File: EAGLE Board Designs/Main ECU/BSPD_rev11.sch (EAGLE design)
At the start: 55 parts, among them Q1 P-CHANNEL_MOSFET_DMP3099L-7, U11 SN74AHC1G09, U17 OPA990IDBVR, U19 OPA990IDBVR, U28 OPA990IDBVR, U29 OPA990IDBVR, U6 OPA990IDBVR, X1 CONNECTOR-4NANO-FIT-VERTICAL-4, X2 CONNECTOR-4NANO-FIT-VERTICAL-4

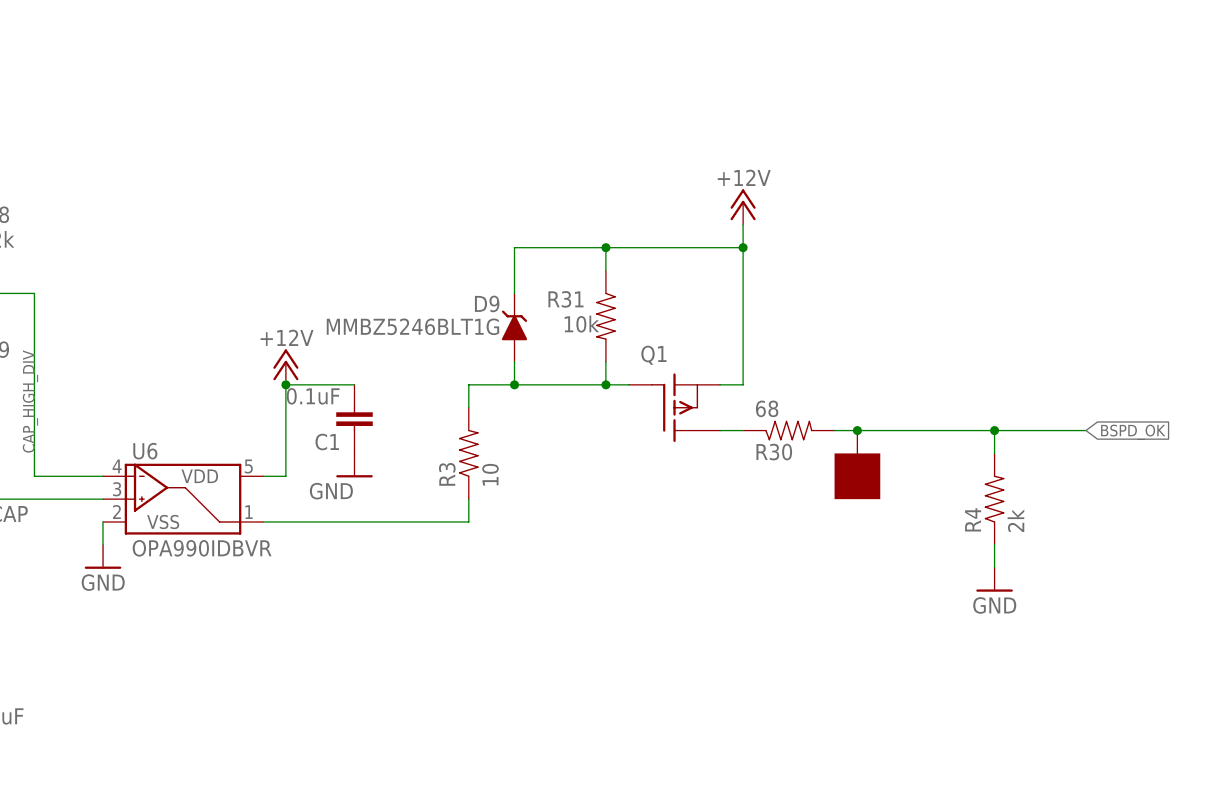
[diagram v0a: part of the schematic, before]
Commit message: Made layout more compact
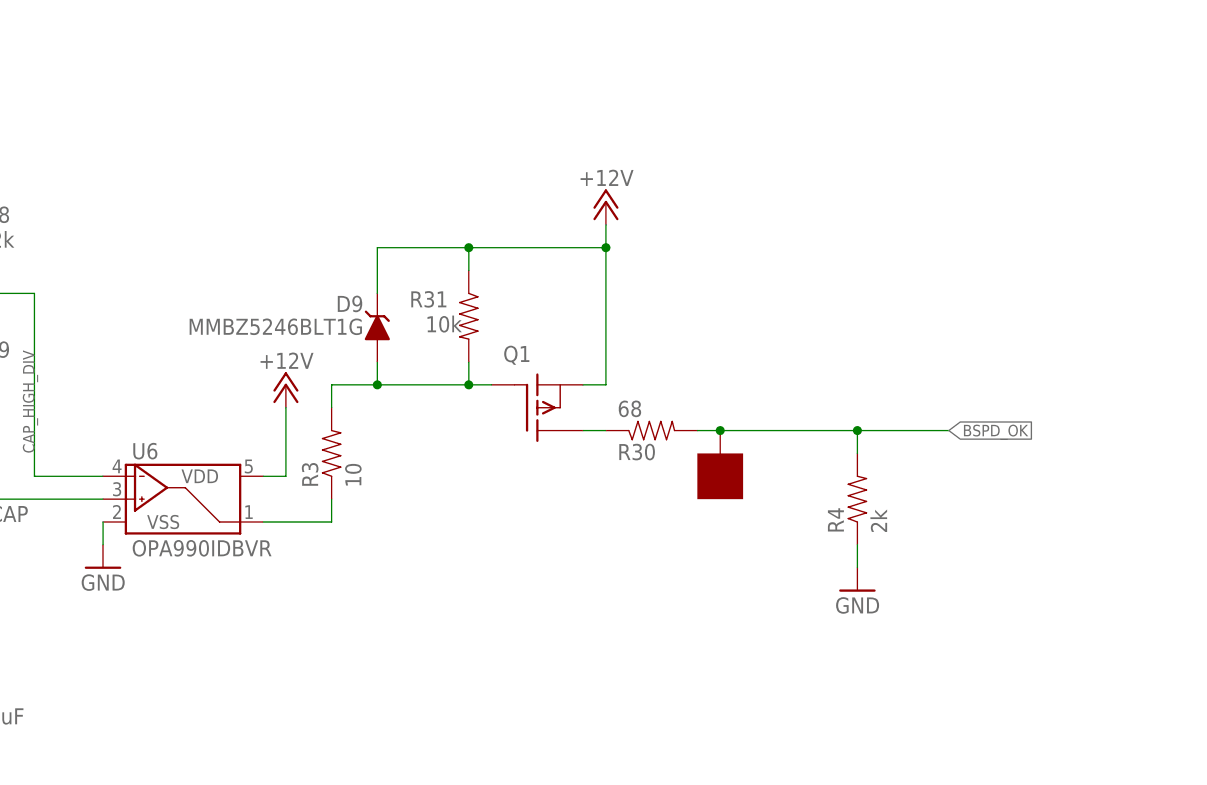
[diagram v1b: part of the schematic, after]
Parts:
- removed C1: 0.1uF, HyTechDevices:CAP0603-CAP
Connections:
- net +12V: no longer C1.2
- net GND: no longer C1.1
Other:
- moved on the sheet: D9, Q1, R3, R30, R31, R4

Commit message: Made more compact, adjusted labels
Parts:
- renumbered U$1 to BRAKE_LOW_DIV, U$2 to CURRENT_LOW_DIV
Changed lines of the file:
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@@
 <part name="R7" library="HyTechDevices" deviceset="RESISTOR" device="0603" value="31600"/>
 <part name="R8" library="HyTechDevices" deviceset="RESISTOR" device="0603" value="5110"/>
-<part name="U$1" library="HyTechDevices" deviceset="SOLDER_PAD" device=""/>
-<part name="U$2" library="HyTechDevices" deviceset="SOLDER_PAD" device=""/>
+<part name="BRAKE_LOW_DIV" library="HyTechDevices" deviceset="SOLDER_PAD" device=""/>
+<part name="CURRENT_LOW_DIV" library="HyTechDevices" deviceset="SOLDER_PAD" device=""/>
 </parts>
 <sheets>
@@
 <attribute name="VALUE" x="104.902" y="158.75" size="1.778" layer="96" rot="R90"/>
 </instance>
-<instance part="U$1" gate="G$1" x="154.94" y="157.48" smashed="yes" rot="R270"/>
-<instance part="U$2" gate="G$1" x="182.88" y="218.44" smashed="yes"/>
+<instance part="BRAKE_LOW_DIV" gate="G$1" x="154.94" y="157.48" smashed="yes" rot="R270"/>
+<instance part="CURRENT_LOW_DIV" gate="G$1" x="182.88" y="218.44" smashed="yes"/>
 </instances>
 <busses>
@@
 <wire x1="167.64" y1="226.06" x2="152.4" y2="226.06" width="0.1524" layer="91"/>
 <junction x="167.64" y="226.06"/>
-<pinref part="U$2" gate="G$1" pin="P$1"/>
+<pinref part="CURRENT_LOW_DIV" gate="G$1" pin="P$1"/>
 <junction x="180.34" y="220.98"/>
 </segment>
@@
 <pinref part="R6" gate="G$1" pin="2"/>
 <junction x="167.64" y="160.02"/>
-<pinref part="U$1" gate="G$1" pin="P$1"/>
+<pinref part="BRAKE_LOW_DIV" gate="G$1" pin="P$1"/>
 <junction x="157.48" y="160.02"/>
 </segment>

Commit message: Routed BSPD circuit, readjusted some components
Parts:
- renumbered U$3 to BSPD_OK
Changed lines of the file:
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@@
 <part name="P+2" library="HyTechSupplies" deviceset="+12V" device=""/>
 <part name="P+8" library="HyTechSupplies" deviceset="+12V" device=""/>
-<part name="U$3" library="HyTechDevices" deviceset="SOLDER_PAD" device=""/>
+<part name="BSPD_OK" library="HyTechDevices" deviceset="SOLDER_PAD" device=""/>
 <part name="R3" library="HyTechDevices" deviceset="RESISTOR" device="0603" value="10"/>
 <part name="REG2" library="HyTechDevices" deviceset="OKI-78SR-5" device="" value="5V"/>
@@
 <attribute name="VALUE" x="80.772" y="77.978" size="1.778" layer="96"/>
 </instance>
-<instance part="U$3" gate="G$1" x="365.76" y="167.64" smashed="yes" rot="R270"/>
+<instance part="BSPD_OK" gate="G$1" x="365.76" y="167.64" smashed="yes" rot="R270"/>
 <instance part="R3" gate="G$1" x="325.12" y="167.64" smashed="yes" rot="R90">
 <attribute name="NAME" x="323.6214" y="163.83" size="1.778" layer="95" rot="R90"/>
@@
 <wire x1="365.76" y1="170.18" x2="368.3" y2="170.18" width="0.1524" layer="91"/>
 <label x="393.7" y="170.18" size="1.27" layer="95" xref="yes"/>
-<pinref part="U$3" gate="G$1" pin="P$1"/>
+<pinref part="BSPD_OK" gate="G$1" pin="P$1"/>
 <junction x="368.3" y="170.18"/>
 <pinref part="R4" gate="G$1" pin="2"/>

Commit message: Changed GND of LEDs, cleaned up routing
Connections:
- removed net GND1: BRAKE.C, BSPD.C, CURRENT.C
- net GND: now also BRAKE.C, BSPD.C, CURRENT.C
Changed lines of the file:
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@@
 <part name="R4" library="HyTechDevices" deviceset="RESISTOR" device="0603" value="2k"/>
 <part name="GND2" library="HyTechSymbols" deviceset="GND" device=""/>
-<part name="GND96" library="HyTechSymbols" deviceset="GND" device=""/>
 <part name="BRAKE" library="HyTechDevices" deviceset="LED" device="-0805" value="Red"/>
 <part name="R35" library="HyTechDevices" deviceset="RESISTOR" device="0603" value="215"/>
@@
 <part name="BRAKE_LOW_DIV" library="HyTechDevices" deviceset="SOLDER_PAD" device=""/>
 <part name="CURRENT_LOW_DIV" library="HyTechDevices" deviceset="SOLDER_PAD" device=""/>
+<part name="GND5" library="HyTechSupplies" deviceset="GND" device=""/>
 </parts>
 <sheets>
@@
 <attribute name="VALUE" x="386.08" y="149.86" size="1.778" layer="96" rot="MR0"/>
 </instance>
-<instance part="GND96" gate="1" x="215.9" y="43.18" smashed="yes">
-<attribute name="VALUE" x="213.36" y="40.64" size="1.778" layer="96"/>
-</instance>
 <instance part="BRAKE" gate="LED" x="203.2" y="50.8" smashed="yes" rot="MR270">
 <attribute name="NAME" x="207.772" y="47.244" size="1.778" layer="95" rot="MR0"/>
@@
 <instance part="BRAKE_LOW_DIV" gate="G$1" x="154.94" y="157.48" smashed="yes" rot="R270"/>
 <instance part="CURRENT_LOW_DIV" gate="G$1" x="182.88" y="218.44" smashed="yes"/>
+<instance part="GND5" gate="1" x="215.9" y="43.18" smashed="yes">
+<attribute name="VALUE" x="213.36" y="40.64" size="1.778" layer="96"/>
+</instance>
 </instances>
 <busses>
@@
 <wire x1="167.64" y1="147.32" x2="167.64" y2="149.86" width="0.1524" layer="91"/>
 <pinref part="R6" gate="G$1" pin="1"/>
+</segment>
+<segment>
+<pinref part="BSPD" gate="LED" pin="C"/>
+<wire x1="208.28" y1="76.2" x2="215.9" y2="76.2" width="0.1524" layer="91"/>
+<wire x1="215.9" y1="76.2" x2="215.9" y2="63.5" width="0.1524" layer="91"/>
+<wire x1="215.9" y1="63.5" x2="215.9" y2="50.8" width="0.1524" layer="91"/>
+<wire x1="215.9" y1="50.8" x2="215.9" y2="45.72" width="0.1524" layer="91"/>
+<pinref part="CURRENT" gate="LED" pin="C"/>
+<wire x1="208.28" y1="63.5" x2="215.9" y2="63.5" width="0.1524" layer="91"/>
+<pinref part="BRAKE" gate="LED" pin="C"/>
+<wire x1="208.28" y1="50.8" x2="215.9" y2="50.8" width="0.1524" layer="91"/>
+<junction x="215.9" y="50.8"/>
+<pinref part="GND5" gate="1" pin="GND"/>
 </segment>
 </net>
@@
 </segment>
 </net>
-<net name="GND1" class="0">
-<segment>
-<pinref part="BSPD" gate="LED" pin="C"/>
-<wire x1="208.28" y1="76.2" x2="215.9" y2="76.2" width="0.1524" layer="91"/>
-<wire x1="215.9" y1="76.2" x2="215.9" y2="63.5" width="0.1524" layer="91"/>
-<pinref part="GND96" gate="1" pin="GND"/>
-<wire x1="215.9" y1="63.5" x2="215.9" y2="50.8" width="0.1524" layer="91"/>
-<wire x1="215.9" y1="50.8" x2="215.9" y2="45.72" width="0.1524" layer="91"/>
-<pinref part="CURRENT" gate="LED" pin="C"/>
-<wire x1="208.28" y1="63.5" x2="215.9" y2="63.5" width="0.1524" layer="91"/>
-<pinref part="BRAKE" gate="LED" pin="C"/>
-<wire x1="208.28" y1="50.8" x2="215.9" y2="50.8" width="0.1524" layer="91"/>
-<junction x="215.9" y="50.8"/>
-</segment>
-</net>
